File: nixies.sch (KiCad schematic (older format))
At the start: 22 parts, among them Q12 Q_NPN_BEC, Q13 Q_NPN_BEC, Q14 Q_NPN_BEC, Q15 Q_NPN_BEC, Q16 Q_NPN_BEC, Q17 Q_NPN_BEC, Q18 Q_NPN_BEC, Q19 Q_NPN_BEC, Q20 Q_NPN_BEC, Q21 Q_NPN_BEC

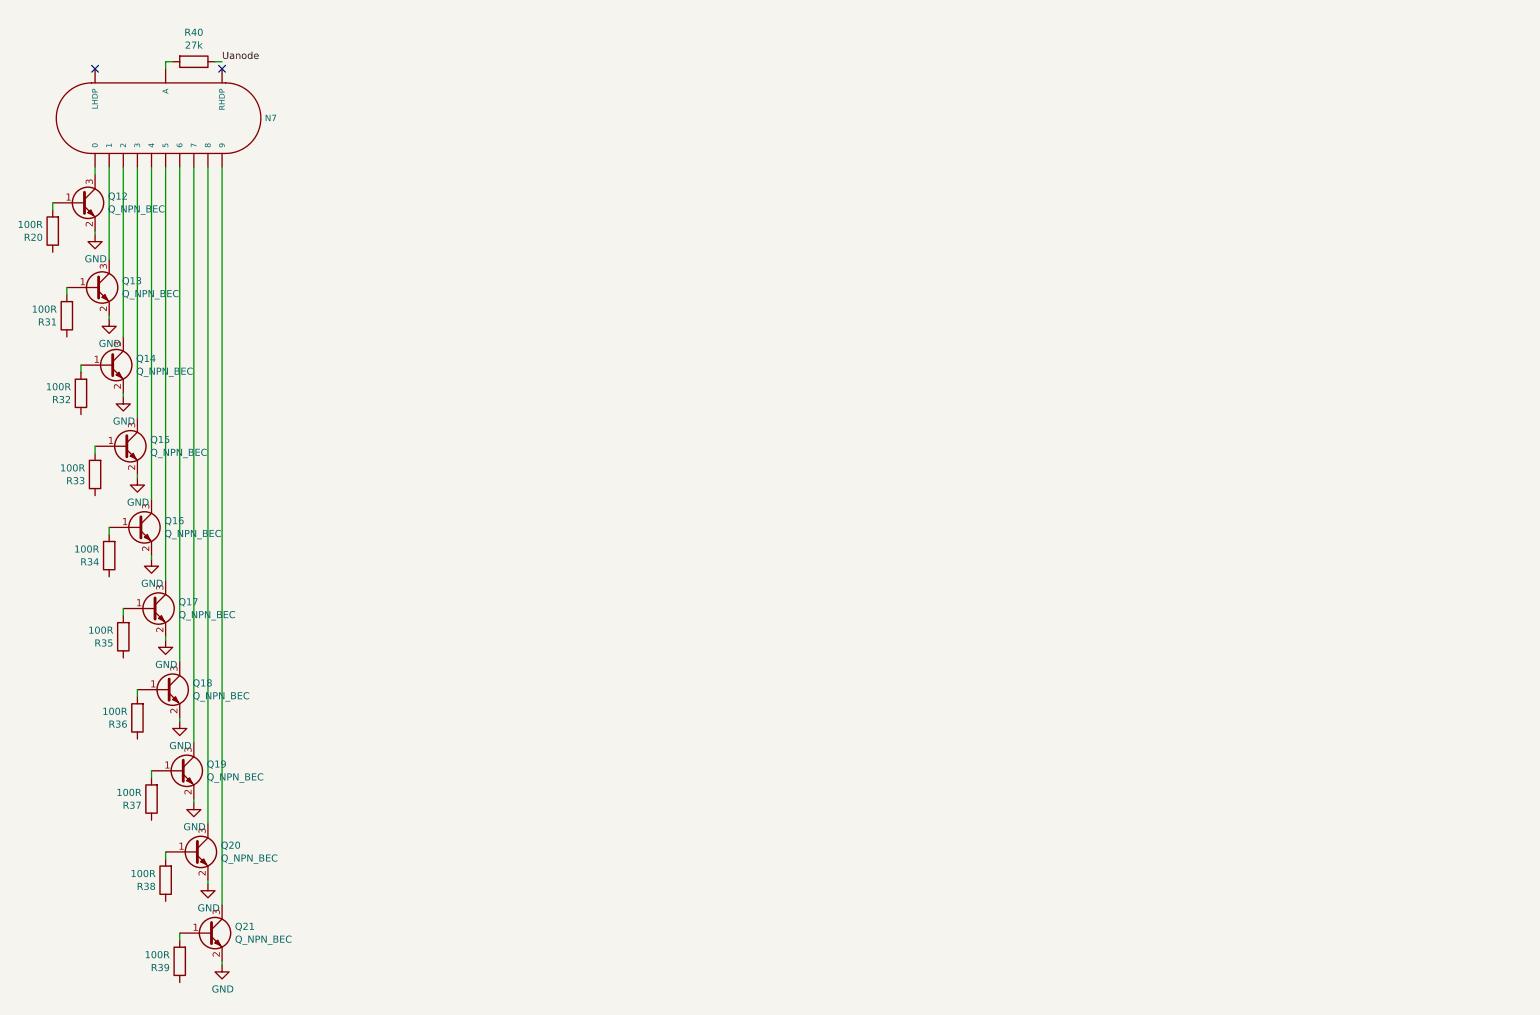
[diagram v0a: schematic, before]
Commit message: Added pin headers for Arduino Mega. Added first two nixies, Changed PCB dimensions
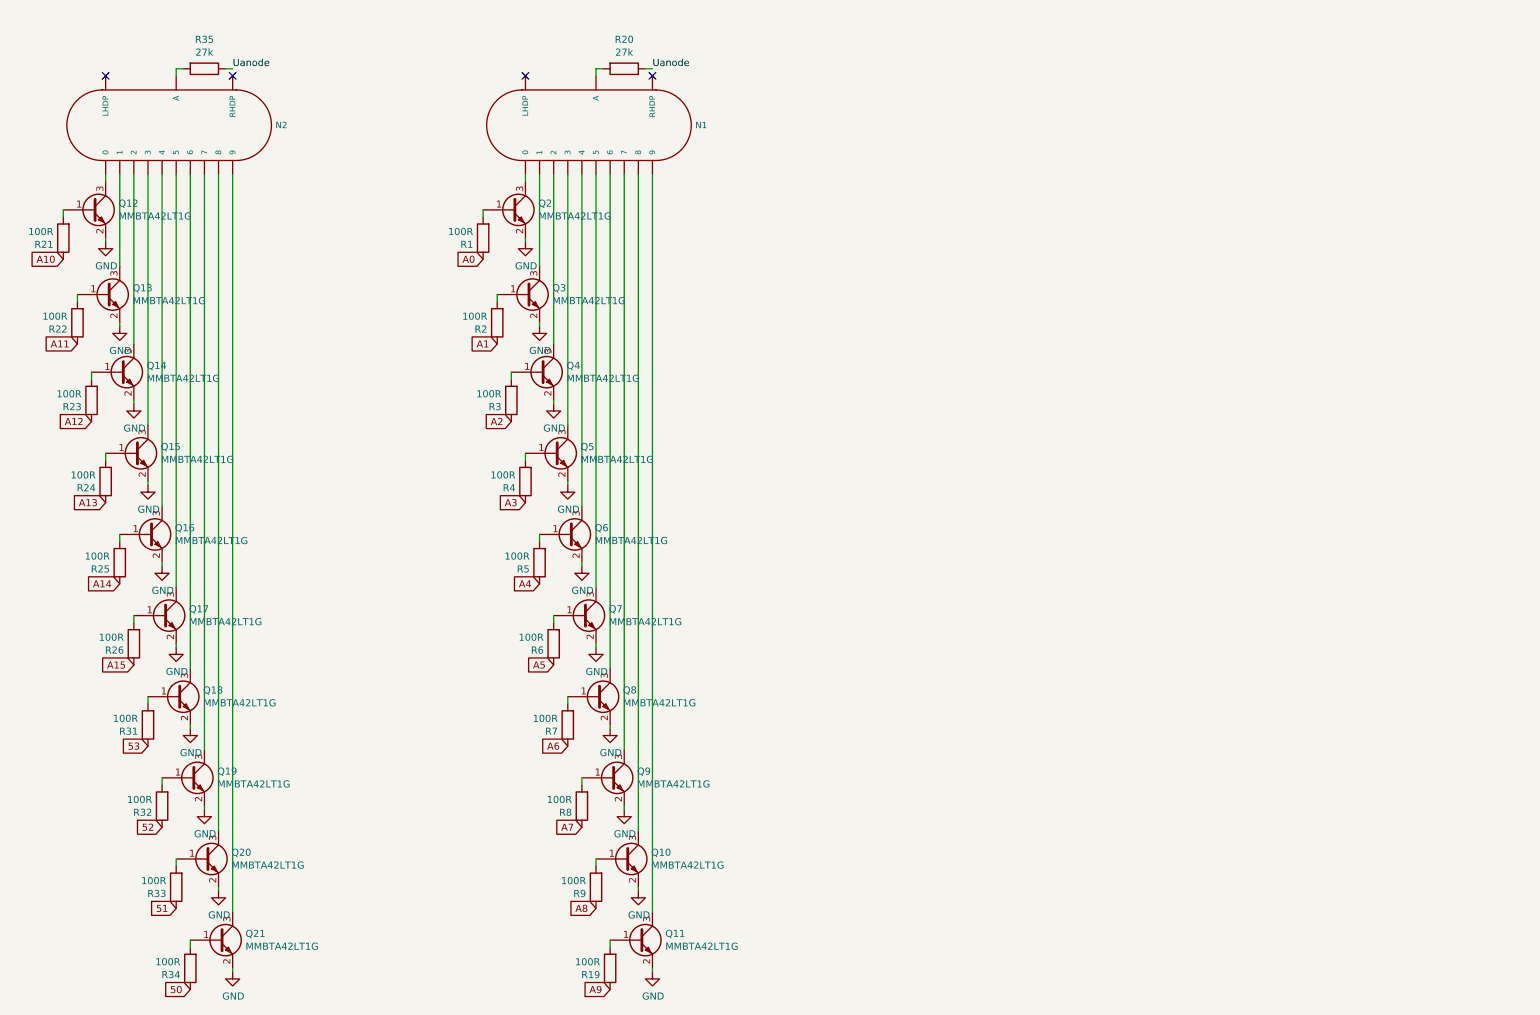
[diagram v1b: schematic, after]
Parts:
- removed N7: ZM1080, riske-lib:ZM1080, symbol NixieClock01A-rescue:ZM1080-mynixies
- removed R36, R37, R38, R39: 100R, Resistor_SMD:R_0603_1608Metric, symbol NixieClock01A-rescue:R-Device
- removed R40: 27k, Resistor_SMD:R_1206_3216Metric, symbol NixieClock01A-rescue:R-Device
- added N1, N2: ZM1080, riske-lib:ZM1080, symbol NixieClock01A-rescue:ZM1080-mynixies
- added Q10, Q11, Q2, Q3, Q4, Q5, Q6, Q7, Q8, Q9: MMBTA42LT1G, Package_TO_SOT_SMD:SOT-23, symbol device:Q_NPN_BEC
- added R1, R19, R2, R21, R22, R23, R24, R25, R26, R3, R4, R5, R6, R7, R8, R9: 100R, Resistor_SMD:R_0603_1608Metric, symbol NixieClock01A-rescue:R-Device
- Q12, Q13, Q14, Q15, Q16, Q17, Q18, Q19, Q20, Q21: value Q_NPN_BEC -> MMBTA42LT1G
- R20, R35: value 100R -> 27k; footprint Resistor_SMD:R_0603_1608Metric -> Resistor_SMD:R_1206_3216Metric
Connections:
- net GND: now also Q10.2 (E), Q11.2 (E), Q2.2 (E), Q3.2 (E), Q4.2 (E), Q5.2 (E), Q6.2 (E), Q7.2 (E), Q8.2 (E), Q9.2 (E)
- net Uanode: now also R20.1, R35.1
- net at Q13.3 (C): now also N2.1
- net at Q21.3 (C): now also N2.11 (9)
- net at Q12.3 (C): now also N2.12 (0)
- net at Q14.3 (C): now also N2.2
- net at Q15.3 (C): now also N2.3
- net at Q16.3 (C): now also N2.5 (4)
- net at Q17.3 (C): now also N2.6 (5)
- net at Q18.3 (C): now also N2.7 (6)
- net at Q19.3 (C): now also N2.8 (7)
- net at Q20.3 (C): now also N2.9 (8)
- net at R20.2: now also N1.13 (A); no longer Q12.1 (B)
- net at R31.2: now also Q18.1 (B); no longer Q13.1 (B)
- net 53: now reaches R31.1
- net at R32.2: now also Q19.1 (B); no longer Q14.1 (B)
- net 52: now reaches R32.1
- net at R33.2: now also Q20.1 (B); no longer Q15.1 (B)
- net 51: now reaches R33.1
- net at R34.2: now also Q21.1 (B); no longer Q16.1 (B)
- net 50: now reaches R34.1
- net at Q17.1 (B): now also R26.2; no longer R35.2
- new net: Q11.1 (B), R19.2
- new net: N1.11 (9), Q11.3 (C)
- new net: Q10.1 (B), R9.2
- new net: N1.9 (8), Q10.3 (C)
- new net: Q9.1 (B), R8.2
- new net: N1.8 (7), Q9.3 (C)
- new net: Q8.1 (B), R7.2
- new net: N1.7 (6), Q8.3 (C)
- new net: Q7.1 (B), R6.2
- new net: N1.6 (5), Q7.3 (C)
- new net: Q6.1 (B), R5.2
- new net: N1.5 (4), Q6.3 (C)
- new net: Q5.1 (B), R4.2
- new net: N1.3, Q5.3 (C)
- new net: Q4.1 (B), R3.2
- new net: N1.2, Q4.3 (C)
- new net: Q3.1 (B), R2.2
- new net: N1.1, Q3.3 (C)
- new net: Q2.1 (B), R1.2
- new net: N1.12 (0), Q2.3 (C)
- new net: Q16.1 (B), R25.2
- new net: Q15.1 (B), R24.2
- new net: Q14.1 (B), R23.2
- new net: Q13.1 (B), R22.2
- new net: Q12.1 (B), R21.2
- new net: N2.13 (A), R35.2
- new net A0: R1.1
- new net A1: R2.1
- new net A10: R21.1
- new net A11: R22.1
- new net A12: R23.1
- new net A13: R24.1
- new net A14: R25.1
- new net A15: R26.1
- new net A2: R3.1
- new net A3: R4.1
- new net A4: R5.1
- new net A5: R6.1
- new net A6: R7.1
- new net A7: R8.1
- new net A8: R9.1
- new net A9: R19.1
- no-connect marks 2 -> 4

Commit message: Added all nixies, added DC-DC converter, basic routing done
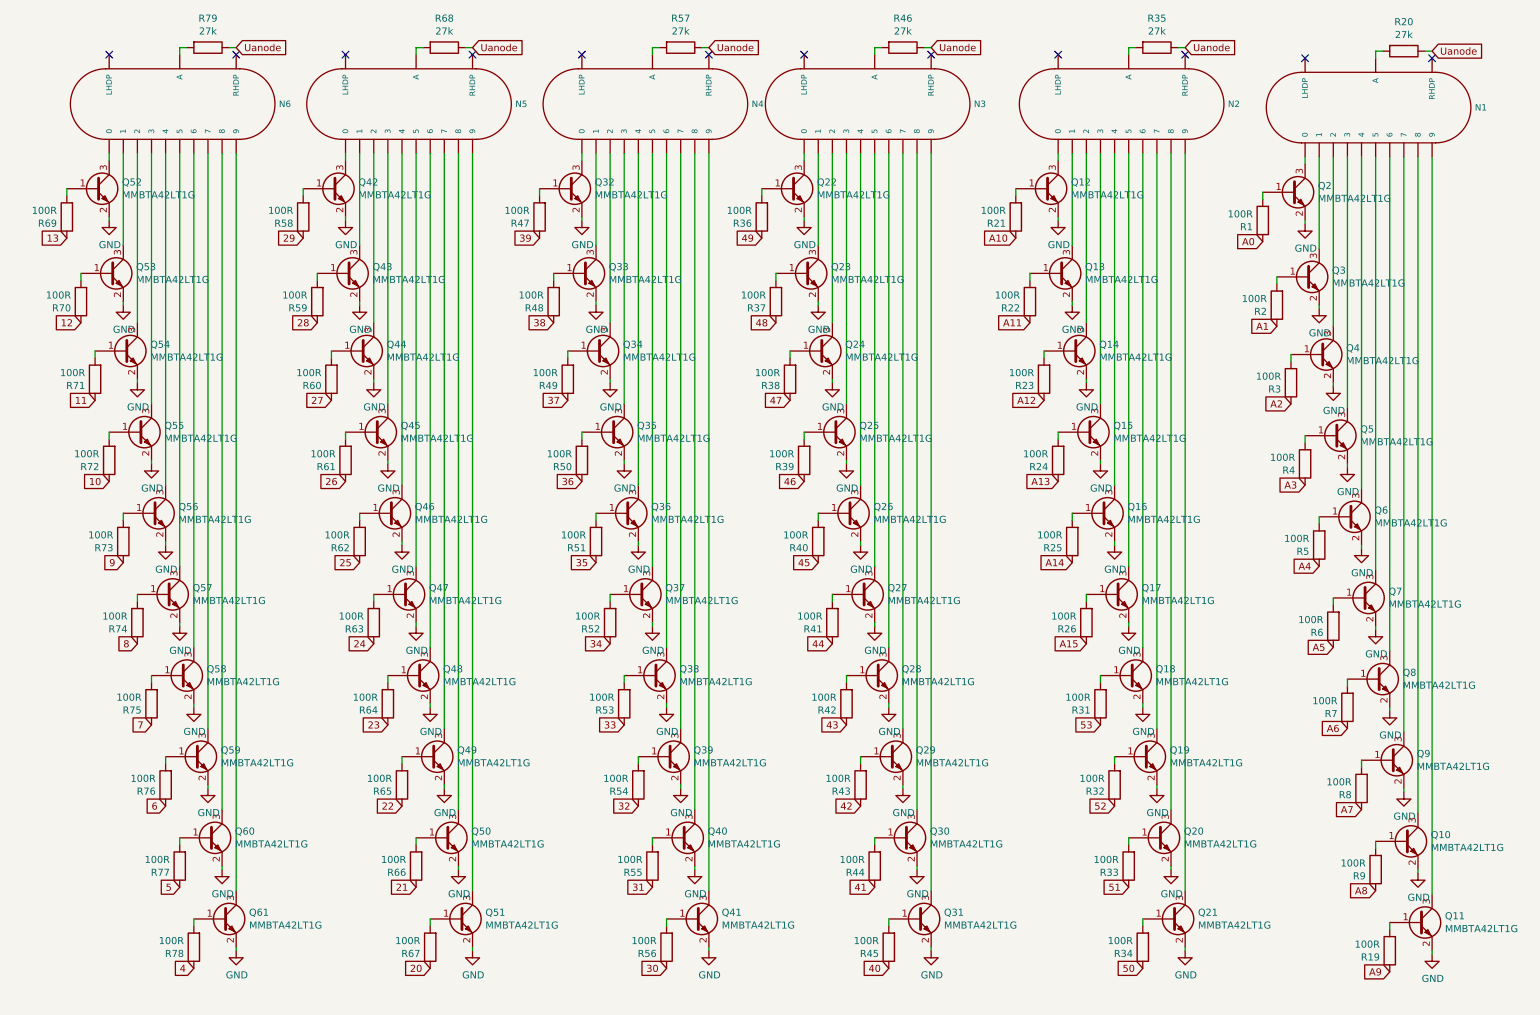
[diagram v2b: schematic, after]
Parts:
- added N3, N4, N5, N6: ZM1080, kicad-footprints-master:ZM1080, symbol NixieClock01A-rescue:ZM1080-mynixies
- added Q22, Q23, Q24, Q25, Q26, Q27, Q28, Q29, Q30, Q31, Q32, Q33, Q34, Q35, Q36, Q37, Q38, Q39, Q40, Q41, Q42, Q43, Q44, Q45, Q46, Q47, Q48, Q49, Q50, Q51, Q52, Q53, Q54, Q55, Q56, Q57, Q58, Q59, Q60, Q61: MMBTA42LT1G, Package_TO_SOT_SMD:SOT-23, symbol device:Q_NPN_BEC
- added R36, R37, R38, R39, R40, R41, R42, R43, R44, R45, R47, R48, R49, R50, R51, R52, R53, R54, R55, R56, R58, R59, R60, R61, R62, R63, R64, R65, R66, R67, R69, R70, R71, R72, R73, R74, R75, R76, R77, R78: 100R, Resistor_SMD:R_0603_1608Metric, symbol NixieClock01A-rescue:R-Device
- added R46, R57, R68, R79: 27k, Resistor_SMD:R_1206_3216Metric, symbol NixieClock01A-rescue:R-Device
- N1, N2: footprint riske-lib:ZM1080 -> kicad-footprints-master:ZM1080
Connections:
- net GND: now also Q22.2 (E), Q23.2 (E), Q24.2 (E), Q25.2 (E), Q26.2 (E), Q27.2 (E), Q28.2 (E), Q29.2 (E), Q30.2 (E), Q31.2 (E), Q32.2 (E), Q33.2 (E), Q34.2 (E), Q35.2 (E), Q36.2 (E), Q37.2 (E), Q38.2 (E), Q39.2 (E), Q40.2 (E), Q41.2 (E), Q42.2 (E), Q43.2 (E), Q44.2 (E), Q45.2 (E), Q46.2 (E), Q47.2 (E), Q48.2 (E), Q49.2 (E), Q50.2 (E), Q51.2 (E), Q52.2 (E), Q53.2 (E), Q54.2 (E), Q55.2 (E), Q56.2 (E), Q57.2 (E), Q58.2 (E), Q59.2 (E), Q60.2 (E), Q61.2 (E)
- net Uanode: now also R46.1, R57.1, R68.1, R79.1
- new net: Q31.1 (B), R45.2
- new net: N3.11 (9), Q31.3 (C)
- new net: Q30.1 (B), R44.2
- new net: N3.9 (8), Q30.3 (C)
- new net: Q29.1 (B), R43.2
- new net: N3.8 (7), Q29.3 (C)
- new net: Q28.1 (B), R42.2
- new net: N3.7 (6), Q28.3 (C)
- new net: Q27.1 (B), R41.2
- new net: N3.6 (5), Q27.3 (C)
- new net: Q26.1 (B), R40.2
- new net: N3.5 (4), Q26.3 (C)
- new net: Q25.1 (B), R39.2
- new net: N3.3, Q25.3 (C)
- new net: Q24.1 (B), R38.2
- new net: N3.2, Q24.3 (C)
- new net: Q23.1 (B), R37.2
- new net: N3.1, Q23.3 (C)
- new net: Q22.1 (B), R36.2
- new net: N3.12 (0), Q22.3 (C)
- new net: N3.13 (A), R46.2
- new net: Q41.1 (B), R56.2
- new net: N4.11 (9), Q41.3 (C)
- new net: Q40.1 (B), R55.2
- new net: N4.9 (8), Q40.3 (C)
- new net: Q39.1 (B), R54.2
- new net: N4.8 (7), Q39.3 (C)
- new net: Q38.1 (B), R53.2
- new net: N4.7 (6), Q38.3 (C)
- new net: Q37.1 (B), R52.2
- new net: N4.6 (5), Q37.3 (C)
- new net: Q36.1 (B), R51.2
- new net: N4.5 (4), Q36.3 (C)
- new net: Q35.1 (B), R50.2
- new net: N4.3, Q35.3 (C)
- new net: Q34.1 (B), R49.2
- new net: N4.2, Q34.3 (C)
- new net: Q33.1 (B), R48.2
- new net: N4.1, Q33.3 (C)
- new net: Q32.1 (B), R47.2
- new net: N4.12 (0), Q32.3 (C)
- new net: N4.13 (A), R57.2
- new net: Q51.1 (B), R67.2
- new net: N5.11 (9), Q51.3 (C)
- new net: Q50.1 (B), R66.2
- new net: N5.9 (8), Q50.3 (C)
- new net: Q49.1 (B), R65.2
- new net: N5.8 (7), Q49.3 (C)
- new net: Q48.1 (B), R64.2
- new net: N5.7 (6), Q48.3 (C)
- new net: Q47.1 (B), R63.2
- new net: N5.6 (5), Q47.3 (C)
- new net: Q46.1 (B), R62.2
- new net: N5.5 (4), Q46.3 (C)
- new net: Q45.1 (B), R61.2
- new net: N5.3, Q45.3 (C)
- new net: Q44.1 (B), R60.2
- new net: N5.2, Q44.3 (C)
- new net: Q43.1 (B), R59.2
- new net: N5.1, Q43.3 (C)
- new net: Q42.1 (B), R58.2
- new net: N5.12 (0), Q42.3 (C)
- new net: N5.13 (A), R68.2
- new net: Q61.1 (B), R78.2
- new net: N6.11 (9), Q61.3 (C)
- new net: Q60.1 (B), R77.2
- new net: N6.9 (8), Q60.3 (C)
- new net: Q59.1 (B), R76.2
- new net: N6.8 (7), Q59.3 (C)
- new net: Q58.1 (B), R75.2
- new net: N6.7 (6), Q58.3 (C)
- new net: Q57.1 (B), R74.2
- new net: N6.6 (5), Q57.3 (C)
- new net: Q56.1 (B), R73.2
- new net: N6.5 (4), Q56.3 (C)
- new net: Q55.1 (B), R72.2
- new net: N6.3, Q55.3 (C)
- new net: Q54.1 (B), R71.2
- new net: N6.2, Q54.3 (C)
- new net: Q53.1 (B), R70.2
- new net: N6.1, Q53.3 (C)
- new net: Q52.1 (B), R69.2
- new net: N6.12 (0), Q52.3 (C)
- new net: N6.13 (A), R79.2
- new net 10: R72.1
- new net 11: R71.1
- new net 12: R70.1
- new net 13: R69.1
- new net 20: R67.1
- new net 21: R66.1
- new net 22: R65.1
- new net 23: R64.1
- new net 24: R63.1
- new net 25: R62.1
- new net 26: R61.1
- new net 27: R60.1
- new net 28: R59.1
- new net 29: R58.1
- new net 30: R56.1
- new net 31: R55.1
- new net 32: R54.1
- new net 33: R53.1
- new net 34: R52.1
- new net 35: R51.1
- new net 36: R50.1
- new net 37: R49.1
- new net 38: R48.1
- new net 39: R47.1
- new net 4: R78.1
- new net 40: R45.1
- new net 41: R44.1
- new net 42: R43.1
- new net 43: R42.1
- new net 44: R41.1
- new net 45: R40.1
- new net 46: R39.1
- new net 47: R38.1
- new net 48: R37.1
- new net 49: R36.1
- new net 5: R77.1
- new net 6: R76.1
- new net 7: R75.1
- new net 8: R74.1
- new net 9: R73.1
- no-connect marks 4 -> 12
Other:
- moved on the sheet: N1, N2, Q10, Q11, Q12, Q13, Q14, Q15, Q16, Q17, Q18, Q19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

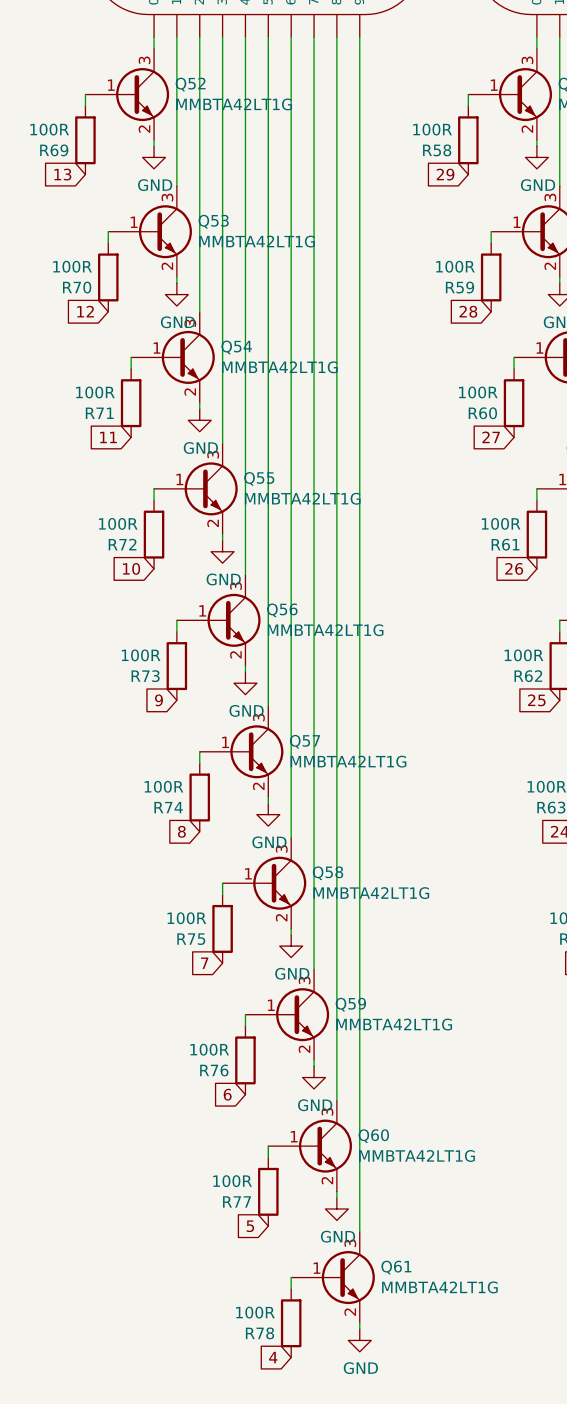
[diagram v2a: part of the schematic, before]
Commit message: Added buttons
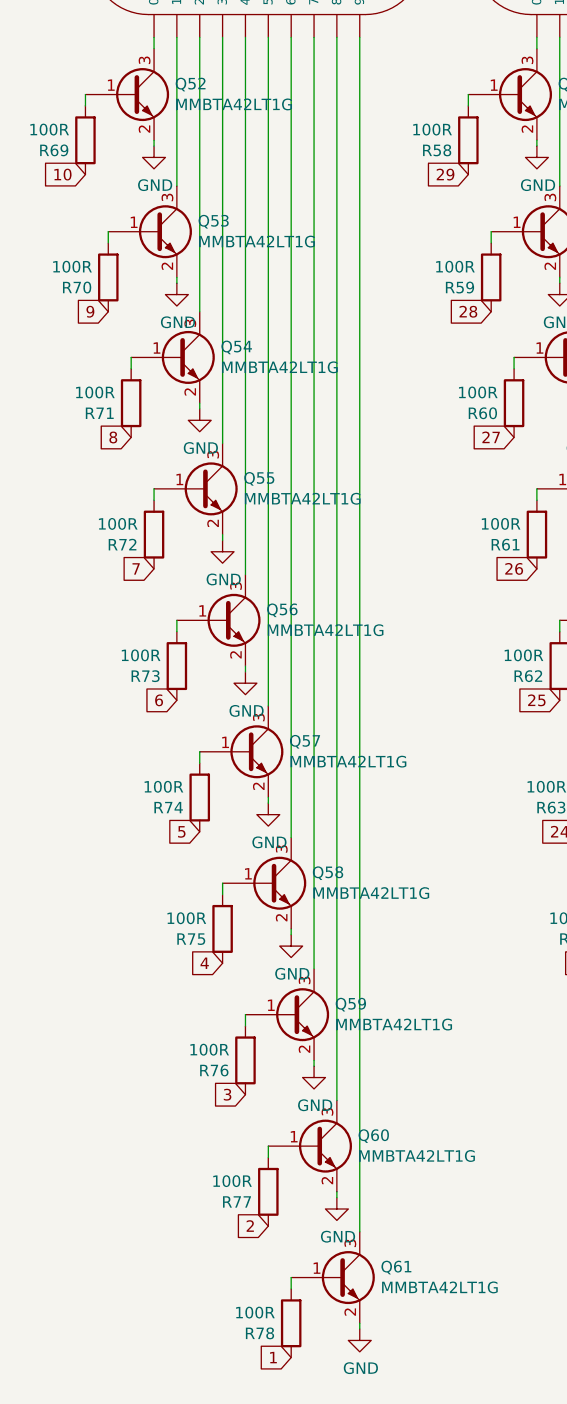
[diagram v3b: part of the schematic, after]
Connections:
- net 11 is gone; now on net 8: R71.1
- net 12 is gone; now on net 9: R70.1
- net 13 is gone; now on net 10: R69.1
- net 10: no longer R72.1
- net 4: now also R75.1; no longer R78.1
- net 5: now also R74.1; no longer R77.1
- net 6: now also R73.1; no longer R76.1
- net 7: now also R72.1; no longer R75.1
- net 8: no longer R74.1
- net 9: no longer R73.1
- new net 1: R78.1
- new net 2: R77.1
- new net 3: R76.1
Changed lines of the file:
@@
 $EndComp
 Text GLabel 1125 3800 0    50   Input ~ 0
+7
+Text GLabel 1225 4375 0    50   Input ~ 0
+6
+Text GLabel 1325 4950 0    50   Input ~ 0
+5
+Text GLabel 1425 5525 0    50   Input ~ 0
+4
+Text GLabel 1525 6100 0    50   Input ~ 0
+3
+Text GLabel 1625 6675 0    50   Input ~ 0
+2
+Text GLabel 1725 7250 0    50   Input ~ 0
+1
+Text GLabel 1025 3225 0    50   Input ~ 0
+8
+Text GLabel 925  2675 0    50   Input ~ 0
+9
+Text GLabel 825  2075 0    50   Input ~ 0
 10
-Text GLabel 1225 4375 0    50   Input ~ 0
-9
-Text GLabel 1325 4950 0    50   Input ~ 0
-8
-Text GLabel 1425 5525 0    50   Input ~ 0
-7
-Text GLabel 1525 6100 0    50   Input ~ 0
-6
-Text GLabel 1625 6675 0    50   Input ~ 0
-5
-Text GLabel 1725 7250 0    50   Input ~ 0
-4
-Text GLabel 1025 3225 0    50   Input ~ 0
-11
-Text GLabel 925  2675 0    50   Input ~ 0
-12
-Text GLabel 825  2075 0    50   Input ~ 0
-13
 Text GLabel 2025 725  2    50   Input ~ 0
 Uanode
